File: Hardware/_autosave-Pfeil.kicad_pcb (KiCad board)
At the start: 4 copper layers, 50 x 6 mm, 62 parts, among them IC1 2536030320001, IC2 nPM1300-CAAA-R, J1 Conn_01x01_Socket, J2 Conn_01x01_Socket, J3 TagConnect, U1 NRF52840-CKAA-R, U2 WSEN-PADS_2511020213301, U3 WSEN-PADS_2511020213301, X1 XTAL 32MHz 8pF, X2 XTAL 32.768kHz 9pF

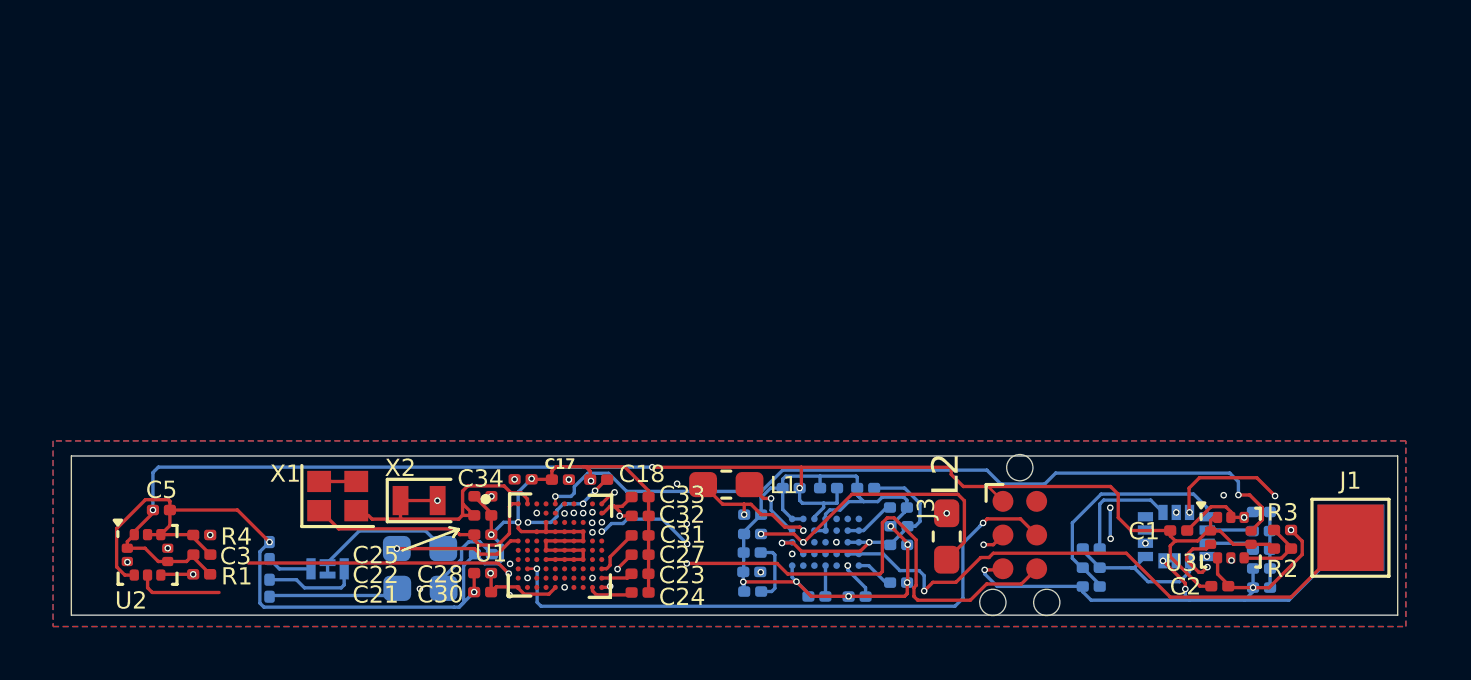
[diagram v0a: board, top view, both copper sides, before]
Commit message: larger pcb
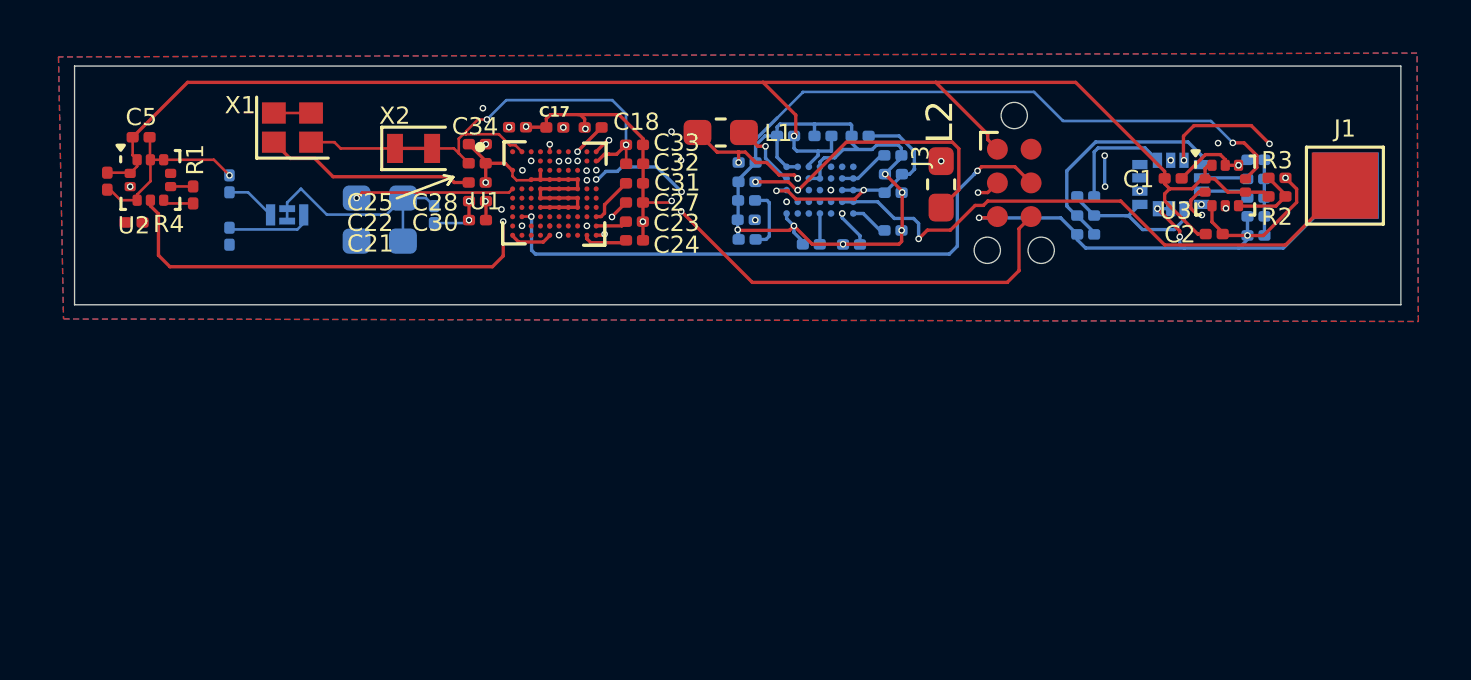
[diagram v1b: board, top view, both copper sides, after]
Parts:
- moved C3 14.5 mm to (127.0, 57.2), turned to -90 degrees
- moved R1 14.3 mm to (130.3, 57.7), turned to -90 degrees
- moved U2 14.1 mm to (128.7, 57.2)
- moved C5 14.1 mm to (128.3, 55.6)
- moved C28 14.0 mm to (141.0, 58.0)
- moved C30 14.0 mm to (141.0, 58.7)
- moved X1 14.0 mm to (134.0, 55.2)
- moved C4 13.9 mm to (131.7, 57.3)
- moved ANT1 13.4 mm to (133.8, 58.5)
- moved C6 13.4 mm to (131.7, 59.3)
- moved L5 13.3 mm to (137.3, 57.8)
- moved C10 13.3 mm to (156.7, 56.2)
- moved C22 13.3 mm to (141.0, 56.5)
- moved C23 13.3 mm to (146.9, 58.7)
- moved C24 13.3 mm to (146.9, 59.4)
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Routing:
- net /I2C_SDA: track 82.6 -> 53.6 mm, vias 6 -> 5
- net /I2C_SCL: track 79.6 -> 57.4 mm, vias 7 -> 6
- net GND: track 114.4 -> 97.2 mm, vias 21 -> 24
- net /PADS_INT01: track 16.4 -> 0.02 mm, vias 2 -> 1
- net /PADS_INT02: track 30.3 -> 22.0 mm
- net VDD: track 22.7 -> 17.1 mm
- net /RF: track 4.95 -> 0.00 mm
- net Net-(U1B-DEC5): track 2.99 -> 0.00 mm
- net Net-(U1A-P0.00/XL1): track 23.0 -> 20.5 mm, vias 3 -> 2
- net /SWDIO: track 25.3 -> 23.1 mm
- net +3V3: track 60.0 -> 62.0 mm, vias 3 -> 1
- net Net-(U2-SA0): track 2.98 -> 1.16 mm, vias 2 -> 0
- net Net-(U1C-XC1): track 9.41 -> 7.99 mm
- net Net-(U1A-ANT): track 4.87 -> 6.02 mm
- net Net-(U1B-DEC4): track 3.81 -> 4.62 mm, vias 3 -> 2
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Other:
- board size 50 x 6 mm -> 50 x 9 mm
